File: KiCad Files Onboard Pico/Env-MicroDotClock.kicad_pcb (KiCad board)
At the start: 2 copper layers, 110 x 80 mm, 105 parts, among them IC1 IS31FL3730-QFLS2-TR, IC2 IS31FL3730-QFLS2-TR, IC3 IS31FL3730-QFLS2-TR, IC4 IS31FL3730-QFLS2-TR, J1 Conn_01x06_Pin, J3 Button, M1 Dip-14 Socket, M2 Dip-14 Socket, M3 Dip-14 Socket, M4 Dip-14 Socket, M5 Dip-14 Socket, M6 Dip-14 Socket, M7 Dip-14 Socket, M8 Dip-14 Socket, Q1 2SC1815, SW1 SW_Push, SW2 SW_Push, SW3 SW_Push, SW4 SW_Push, SW5 SW_Push, U1 Si7021-A20, U2 SOT-23-5 5.5V 3.3V 500mA, U3 DS3231M, U4 RP2040, Y1 3225_4P 12MHz

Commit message: sync push
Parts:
- moved R21 28.8 mm to (93.5, 47.0)
- moved R4 27.4 mm to (55.5, 69.5), turned to 180 degrees
- moved C30 27.0 mm to (89.9, 59.1)
- moved C31 27.0 mm to (89.9, 61.1)
- moved C26 27.0 mm to (87.0, 61.1)
- moved C27 27.0 mm to (87.0, 63.0)
- moved C28 27.0 mm to (87.0, 65.0)
- moved C29 27.0 mm to (87.0, 67.0)
- moved C24 27.0 mm to (84.1, 67.0)
- moved R3 26.9 mm to (55.5, 63.0)
- moved R18 17.8 mm to (121.0, 79.5), turned to 0 degrees
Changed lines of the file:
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@@
   (net 154 "unconnected-(U1-PAD-Pad7)")
   (footprint "Resistor_SMD:R_0805_2012Metric" (layer "F.Cu")
-    (at 82.27 60.85)
+    (at 55.5 63)
     (descr "Resistor SMD 0805 (2012 Metric), square (rectangular) end terminal, IPC_7351 nominal, (Body size source: IPC-SM-782 page 72, https://www.pcb-3d.com/wordpress/wp-content/uploads/ipc-sm-782a_amendment_1_and_2.pdf), generated with kicad-footprint-generator")
     (tags "resistor")
@@
   )
   (footprint "Capacitor_SMD:C_0402_1005Metric" (layer "F.Cu")
-    (at 61.525 56.125)
+    (at 87 65)
     (descr "Capacitor SMD 0402 (1005 Metric), square (rectangular) end terminal, IPC_7351 nominal, (Body size source: IPC-SM-782 page 76, https://www.pcb-3d.com/wordpress/wp-content/uploads/ipc-sm-782a_amendment_1_and_2.pdf), generated with kicad-footprint-generator")
     (tags "capacitor")
@@
   )
   (footprint "Resistor_SMD:R_0402_1005Metric" (layer "F.Cu")
-    (at 108.1 67.19 90)
+    (at 121 79.5)
     (descr "Resistor SMD 0402 (1005 Metric), square (rectangular) end terminal, IPC_7351 nominal, (Body size source: IPC-SM-782 page 72, https://www.pcb-3d.com/wordpress/wp-content/uploads/ipc-sm-782a_amendment_1_and_2.pdf), generated with kicad-footprint-generator")
     (tags "resistor")
@@
     (property "ki_keywords" "R res resistor")
     (attr smd)
-    (fp_text reference "R18" (at 0 -1.17 90) (layer "F.SilkS")
+    (fp_text reference "R18" (at 0 -1.17) (layer "F.SilkS")
         (effects (font (size 1 1) (thickness 0.15)))
     )
-    (fp_text value "1K 0402" (at 0 1.17 90) (layer "F.Fab")
+    (fp_text value "1K 0402" (at 0 1.17) (layer "F.Fab")
         (effects (font (size 1 1) (thickness 0.15)))
     )
-    (fp_text user "${REFERENCE}" (at 0 0 90) (layer "F.Fab")
+    (fp_text user "${REFERENCE}" (at 0 0) (layer "F.Fab")
         (effects (font (size 0.26 0.26) (thickness 0.04)))
     )
@@
     (fp_line (start 0.525 0.27) (end -0.525 0.27)
       (stroke (width 0.1) (type solid)) (layer "F.Fab"))
-    (pad "1" smd roundrect (at -0.51 0 90) (size 0.54 0.64) (layers "F.Cu" "F.Paste" "F.Mask") (roundrect_rratio 0.25)
+    (pad "1" smd roundrect (at -0.51 0) (size 0.54 0.64) (layers "F.Cu" "F.Paste" "F.Mask") (roundrect_rratio 0.25)
       (net 16 "/Onboard Pico/QSPI_SS") (pintype "passive"))
-    (pad "2" smd roundrect (at 0.51 0 90) (size 0.54 0.64) (layers "F.Cu" "F.Paste" "F.Mask") (roundrect_rratio 0.25)
+    (pad "2" smd roundrect (at 0.51 0) (size 0.54 0.64) (layers "F.Cu" "F.Paste" "F.Mask") (roundrect_rratio 0.25)
       (net 101 "/Onboard Pico/~{USB_BOOT}") (pintype "passive"))
     (model "${KICAD6_3DMODEL_DIR}/Resistor_SMD.3dshapes/R_0402_1005Metric.wrl"
@@
   )
   (footprint "Capacitor_SMD:C_0402_1005Metric" (layer "F.Cu")
-    (at 64.395 52.185)
+    (at 89.87 61.06)
     (descr "Capacitor SMD 0402 (1005 Metric), square (rectangular) end terminal, IPC_7351 nominal, (Body size source: IPC-SM-782 page 76, https://www.pcb-3d.com/wordpress/wp-content/uploads/ipc-sm-782a_amendment_1_and_2.pdf), generated with kicad-footprint-generator")
     (tags "capacitor")
@@
   )
   (footprint "Capacitor_SMD:C_0402_1005Metric" (layer "F.Cu")
-    (at 61.525 52.185)
+    (at 87 61.06)
     (descr "Capacitor SMD 0402 (1005 Metric), square (rectangular) end terminal, IPC_7351 nominal, (Body size source: IPC-SM-782 page 76, https://www.pcb-3d.com/wordpress/wp-content/uploads/ipc-sm-782a_amendment_1_and_2.pdf), generated with kicad-footprint-generator")
     (tags "capacitor")
@@
   )
   (footprint "Capacitor_SMD:C_0402_1005Metric" (layer "F.Cu")
-    (at 61.525 58.095)
+    (at 87 66.97)
     (descr "Capacitor SMD 0402 (1005 Metric), square (rectangular) end terminal, IPC_7351 nominal, (Body size source: IPC-SM-782 page 76, https://www.pcb-3d.com/wordpress/wp-content/uploads/ipc-sm-782a_amendment_1_and_2.pdf), generated with kicad-footprint-generator")
     (tags "capacitor")
@@
   )
   (footprint "Capacitor_SMD:C_0402_1005Metric" (layer "F.Cu")
-    (at 64.395 50.215)
+    (at 89.87 59.09)
     (descr "Capacitor SMD 0402 (1005 Metric), square (rectangular) end terminal, IPC_7351 nominal, (Body size source: IPC-SM-782 page 76, https://www.pcb-3d.com/wordpress/wp-content/uploads/ipc-sm-782a_amendment_1_and_2.pdf), generated with kicad-footprint-generator")
     (tags "capacitor")
@@
   )
   (footprint "Resistor_SMD:R_0402_1005Metric" (layer "F.Cu")
-    (at 114.07 67.19 90)
+    (at 93.5 47 90)
     (descr "Resistor SMD 0402 (1005 Metric), square (rectangular) end terminal, IPC_7351 nominal, (Body size source: IPC-SM-782 page 72, https://www.pcb-3d.com/wordpress/wp-content/uploads/ipc-sm-782a_amendment_1_and_2.pdf), generated with kicad-footprint-generator")
     (tags "resistor")
@@
   )
   (footprint "Resistor_SMD:R_0805_2012Metric" (layer "F.Cu")
-    (at 82.27 63.8)
+    (at 55.5 69.5 180)
     (descr "Resistor SMD 0805 (2012 Metric), square (rectangular) end terminal, IPC_7351 nominal, (Body size source: IPC-SM-782 page 72, https://www.pcb-3d.com/wordpress/wp-content/uploads/ipc-sm-782a_amendment_1_and_2.pdf), generated with kicad-footprint-generator")
     (tags "resistor")
@@
     (fp_line (start 1 0.625) (end -1 0.625)
       (stroke (width 0.1) (type solid)) (layer "F.Fab"))
-    (pad "1" smd roundrect (at -0.9125 0) (size 1.025 1.4) (layers "F.Cu" "F.Paste" "F.Mask") (roundrect_rratio 0.243902)
+    (pad "1" smd roundrect (at -0.9125 0 180) (size 1.025 1.4) (layers "F.Cu" "F.Paste" "F.Mask") (roundrect_rratio 0.243902)
       (net 109 "Buzzer GPIO") (pintype "passive"))
-    (pad "2" smd roundrect (at 0.9125 0) (size 1.025 1.4) (layers "F.Cu" "F.Paste" "F.Mask") (roundrect_rratio 0.243902)
+    (pad "2" smd roundrect (at 0.9125 0 180) (size 1.025 1.4) (layers "F.Cu" "F.Paste" "F.Mask") (roundrect_rratio 0.243902)
       (net 108 "Net-(Q1-B)") (pintype "passive"))
     (model "${KICAD6_3DMODEL_DIR}/Resistor_SMD.3dshapes/R_0805_2012Metric.wrl"
@@
   )
   (footprint "Capacitor_SMD:C_0402_1005Metric" (layer "F.Cu")
-    (at 61.525 54.155)
+    (at 87 63.03)
     (descr "Capacitor SMD 0402 (1005 Metric), square (rectangular) end terminal, IPC_7351 nominal, (Body size source: IPC-SM-782 page 76, https://www.pcb-3d.com/wordpress/wp-content/uploads/ipc-sm-782a_amendment_1_and_2.pdf), generated with kicad-footprint-generator")
     (tags "capacitor")
@@
   )
   (footprint "Capacitor_SMD:C_0402_1005Metric" (layer "F.Cu")
-    (at 58.655 58.095)
+    (at 84.13 66.97)
     (descr "Capacitor SMD 0402 (1005 Metric), square (rectangular) end terminal, IPC_7351 nominal, (Body size source: IPC-SM-782 page 76, https://www.pcb-3d.com/wordpress/wp-content/uploads/ipc-sm-782a_amendment_1_and_2.pdf), generated with kicad-footprint-generator")
     (tags "capacitor")

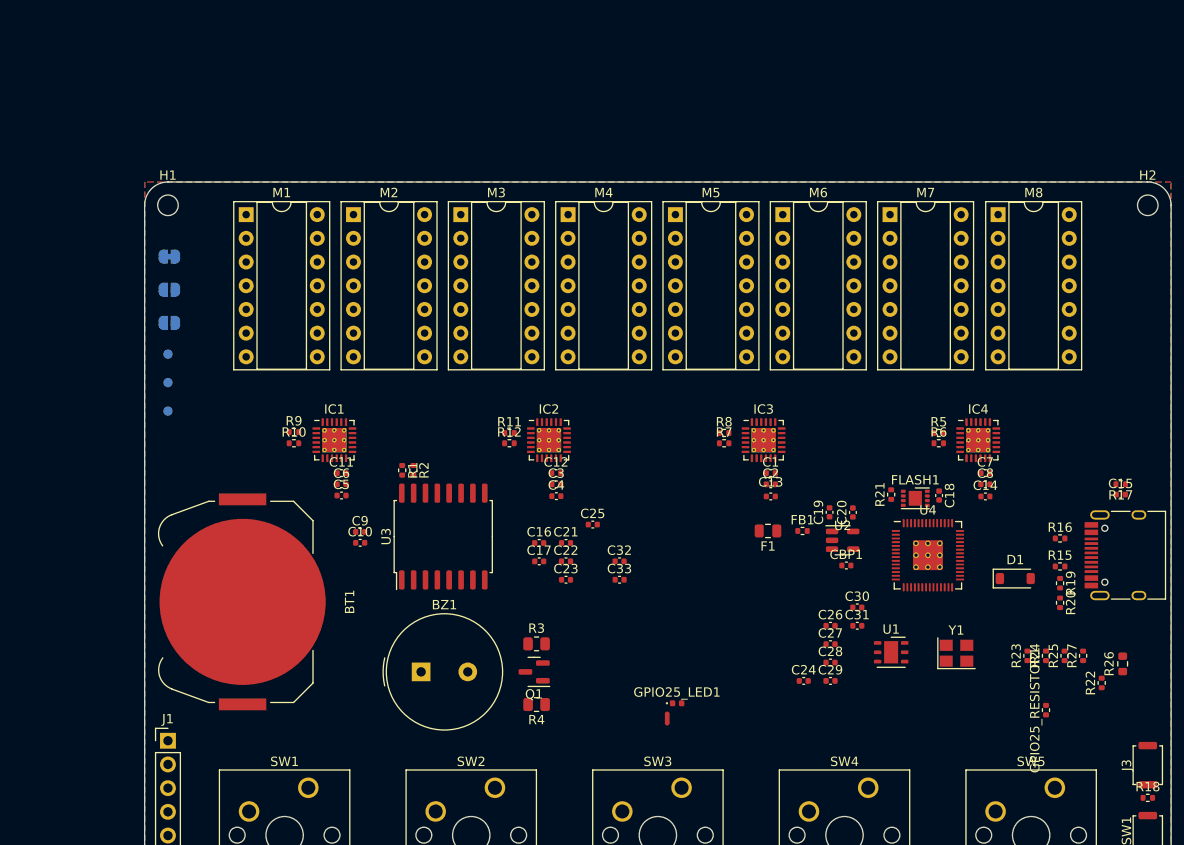
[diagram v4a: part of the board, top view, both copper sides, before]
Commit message: Finished V1 Placement of onboard pico
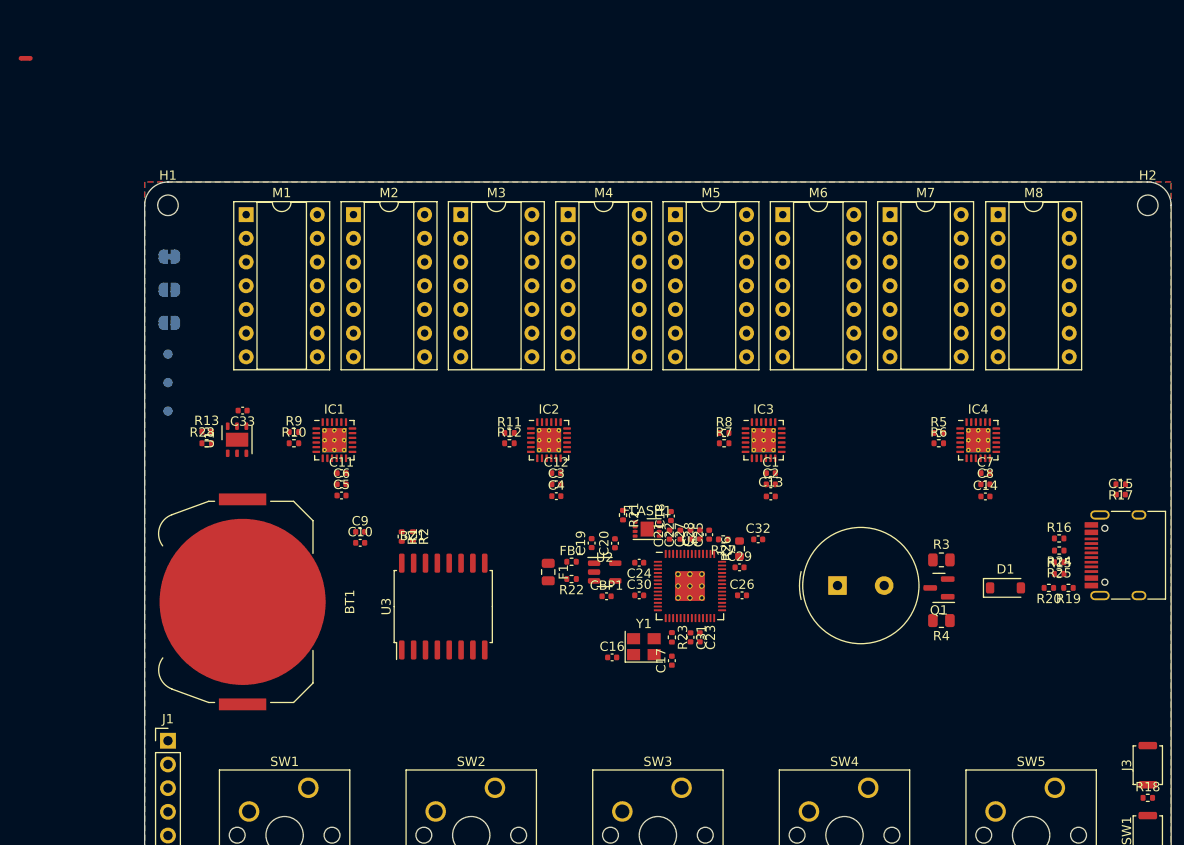
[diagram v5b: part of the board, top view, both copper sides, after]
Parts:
- removed GPIO25_LED1: LED_0402, LED_SMD:LED_0402_1005Metric
- removed GPIO25_RESISTOR1: 470 0402, Resistor_SMD:R_0402_1005Metric
- added R13: 0402 10K, Resistor_SMD:R_0402_1005Metric, F.Cu at (20.1, 40.2)
- added R28: 0402 10K, Resistor_SMD:R_0402_1005Metric, F.Cu at (20.1, 41.5)
- C33: value 10uf 0402 -> 0402 0.1uF
- moved NT1 98.7 mm to (0.75, 0.25), turned to 0 degrees
- moved U1 73.7 mm to (23.4, 41.1), turned to 90 degrees
- moved R22 57.9 mm to (59.2, 56.0), turned to 180 degrees
- moved BZ1 45.6 mm to (87.8, 56.8)
- moved R3 44.3 mm to (98.9, 54.0)
- moved R4 44.3 mm to (98.9, 60.5)
- moved Q1 44.3 mm to (98.6, 57.0)
- moved C33 44.3 mm to (24.0, 38.0), turned to 180 degrees
- moved R26 42.9 mm to (77.2, 52.8)
- moved R27 40.5 mm to (75.5, 51.8), turned to 180 degrees
- moved R23 38.2 mm to (70.0, 62.3), turned to -90 degrees
- moved Y1 33.5 mm to (67.0, 63.3)
- moved FLASH1 28.9 mm to (67.3, 50.7)
- moved C18 28.8 mm to (69.9, 49.3), turned to 90 degrees
- moved R21 28.8 mm to (64.8, 49.2), turned to -90 degrees
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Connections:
- BT1 pad 2: GND -> DEBUG-GND
- C1 pad 2: GND -> DEBUG-GND
- C10 pad 2: GND -> DEBUG-GND
- C11 pad 2: GND -> DEBUG-GND
- C12 pad 2: GND -> DEBUG-GND
- C13 pad 2: GND -> DEBUG-GND
- C14 pad 2: GND -> DEBUG-GND
- C15 pad 1: GND -> DEBUG-GND
- C16 pad 1: GND -> DEBUG-GND
- C17 pad 1: GND -> DEBUG-GND
- C18 pad 2: GND -> DEBUG-GND
- C19 pad 2: GND -> DEBUG-GND
- C2 pad 2: GND -> DEBUG-GND
- C20 pad 2: GND -> DEBUG-GND
- C21 pad 2: GND -> DEBUG-GND
- C22 pad 2: GND -> DEBUG-GND
- C23 pad 2: GND -> DEBUG-GND
- C24 pad 2: GND -> DEBUG-GND
- C25 pad 2: GND -> DEBUG-GND
- C26 pad 2: GND -> DEBUG-GND
- C27 pad 2: GND -> DEBUG-GND
- C28 pad 2: GND -> DEBUG-GND
- C29 pad 2: GND -> DEBUG-GND
- C3 pad 2: GND -> DEBUG-GND
- C30 pad 2: GND -> DEBUG-GND
- C31 pad 2: GND -> DEBUG-GND
- C32 pad 2: GND -> DEBUG-GND
- C33 pad 1: +3V3 -> DEBUG-GND
- C33 pad 2: GND -> +3V3
- C4 pad 2: GND -> DEBUG-GND
- C5 pad 2: GND -> DEBUG-GND
- C6 pad 2: GND -> DEBUG-GND
- C7 pad 2: GND -> DEBUG-GND
- C8 pad 2: GND -> DEBUG-GND
- C9 pad 2: GND -> DEBUG-GND
- CBP1 pad 2: GND -> DEBUG-GND
- FLASH1 pad 4: GND -> DEBUG-GND
- FLASH1 pad 9: GND -> DEBUG-GND
- IC1 pad 1: GPIO0 -> GPIO16
- IC1 pad 2: GPIO1 -> GPIO17
- IC1 pad 20: GND -> DEBUG-GND
- IC1 pad 25: GND -> DEBUG-GND
- IC2 pad 20: GND -> DEBUG-GND
- IC2 pad 25: GND -> DEBUG-GND
- IC2 pad 6: GND -> DEBUG-GND
- IC3 pad 20: GND -> DEBUG-GND
- IC3 pad 25: GND -> DEBUG-GND
- IC4 pad 20: GND -> DEBUG-GND
- IC4 pad 25: GND -> DEBUG-GND
- J1 pad 1: RX -> GPIO1
- J1 pad 2: GND -> DEBUG-GND
- J1 pad 3: TX -> GPIO0
- J3 pad 2: GND -> DEBUG-GND
- NT1 pad 1: GND -> DEBUG-GND
- Q1 pad 2: GND -> DEBUG-GND
- R10 pad 2: GPIO1 -> GPIO17
- R15 pad 1: GND -> DEBUG-GND
- R16 pad 1: GND -> DEBUG-GND
- R17 pad 2: GND -> DEBUG-GND
- R20 pad 2: GND -> DEBUG-GND
- R9 pad 2: GPIO0 -> GPIO16
- RSW1 pad 1: GND -> DEBUG-GND
- SW1 pad 2: GND -> DEBUG-GND
- SW2 pad 2: GND -> DEBUG-GND
- SW3 pad 2: GND -> DEBUG-GND
- SW4 pad 2: GND -> DEBUG-GND
- SW5 pad 2: GND -> DEBUG-GND
- U1 pad 2: GND -> DEBUG-GND
- U2 pad 2: GND -> DEBUG-GND
- U3 pad 10: GND -> DEBUG-GND
- U3 pad 11: GND -> DEBUG-GND
- U3 pad 12: GND -> DEBUG-GND
- U3 pad 13: GND -> DEBUG-GND
- U3 pad 5: GND -> DEBUG-GND
- U3 pad 6: GND -> DEBUG-GND
- U3 pad 7: GND -> DEBUG-GND
- U3 pad 8: GND -> DEBUG-GND
- U3 pad 9: GND -> DEBUG-GND
- U4 pad 19: GND -> DEBUG-GND
- U4 pad 24: /Onboard Pico/SWCLK -> SWCLK
- U4 pad 25: /Onboard Pico/SWD -> SWDIO
- U4 pad 57: GND -> DEBUG-GND
- USB1 pad 1: GND -> DEBUG-GND
- USB1 pad 12: GND -> DEBUG-GND
- Y1 pad 2: GND -> DEBUG-GND
- Y1 pad 4: GND -> DEBUG-GND
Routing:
- added copper zone on B.Cu, net DEBUG-GND
- added copper zone on F.Cu, net DEBUG-GND
- removed copper zone on B.Cu, net GND
- removed copper zone on F.Cu, net GND

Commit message: Finished V2 placement and base wireing of RP2040
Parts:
- removed C32: 2.2uF 0402, Capacitor_SMD:C_0402_1005Metric
- removed R26: 200 0603, Resistor_SMD:R_0603_1608Metric
- removed R27: 1 0402, Resistor_SMD:R_0402_1005Metric
- moved R18 51.9 mm to (77.0, 52.0)
- moved R24 41.0 mm to (71.1, 60.2)
- moved R25 41.0 mm to (71.1, 61.2)
- moved FB1 23.9 mm to (79.9, 66.2), turned to 90 degrees
- moved F1 23.6 mm to (76.5, 68.3), turned to 180 degrees
- moved C19 21.8 mm to (79.9, 63.8)
- moved R22 21.4 mm to (80.0, 61.3), turned to -90 degrees
- moved C20 18.9 mm to (76.5, 66.2), turned to 0 degrees
- moved C28 16.8 mm to (58.1, 59.2), turned to 180 degrees
- moved C27 16.6 mm to (63.6, 65.7), turned to -90 degrees
- moved U2 15.9 mm to (76.5, 63.2), turned to 180 degrees
- moved C17 15.6 mm to (56.1, 57.6), turned to 0 degrees
- moved C23 15.0 mm to (58.1, 60.2), turned to 180 degrees
- moved C16 14.9 mm to (56.1, 51.6), turned to 180 degrees
- moved C29 14.4 mm to (63.1, 52.2), turned to 90 degrees
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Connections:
- U4 pad 43: Net-(U4-ADC_AVDD) -> +3V3
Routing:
- net +3V3: track 0.00 -> 101.5 mm, vias 0 -> 4
- net Net-(BT1-+): track 0.00 -> 35.9 mm
- net Net-(USB1-SHIELD): track 0.00 -> 20.9 mm
- net VCC: track 0.00 -> 17.0 mm
- net +1V1: track 0.00 -> 12.8 mm, vias 0 -> 2
- net VSYS: track 0.00 -> 12.6 mm
- net XIN: track 0.00 -> 10.9 mm
- net /Onboard Pico/QSPI_SS: track 0.00 -> 10.6 mm
- net /Onboard Pico/QSPI_SD1: track 0.00 -> 9.97 mm
- net /Onboard Pico/QSPI_SD2: track 0.00 -> 9.39 mm
- net /Onboard Pico/QSPI_SD3: track 0.00 -> 7.84 mm
- net GPIO8: track 0.00 -> 7.31 mm
- net /Onboard Pico/QSPI_SCLK: track 0.00 -> 7.18 mm
- net /Onboard Pico/QSPI_SD0: track 0.00 -> 6.39 mm
- net GPIO13: track 0.00 -> 4.39 mm
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- added copper zone on F.Cu, net +1V1
- added copper zone on B.Cu, net +3V3
- added copper zone on F.Cu, net +3V3
- added copper zone on F.Cu, net /Onboard Pico/QSPI_SS
- added copper zone on F.Cu, net Net-(C17-Pad2)

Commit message: fulkly wired v2
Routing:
- net /Onboard Pico/~{USB_BOOT}: track 0.00 -> 187.2 mm, vias 0 -> 4
- net +3V3: track 101.5 -> 235.2 mm, vias 4 -> 17
- net USB_D+: track 0.00 -> 131.8 mm, vias 0 -> 4
- net USB_D-: track 0.00 -> 131.0 mm, vias 0 -> 3
- net VBUS: track 0.00 -> 126.3 mm, vias 0 -> 1
- net VCC: track 17.0 -> 130.1 mm, vias 0 -> 1
- net GPIO6: track 2.37 -> 102.3 mm, vias 0 -> 1
- net GPIO3: track 1.98 -> 89.2 mm, vias 0 -> 3
- net GPIO2: track 2.19 -> 83.3 mm, vias 0 -> 2
- net IC1R3: track 0.00 -> 75.8 mm, vias 0 -> 2
- net GPIO0: track 0.00 -> 71.5 mm, vias 0 -> 2
- net /Onboard Pico/RUN: track 0.00 -> 71.1 mm
- net IC4R4: track 0.00 -> 65.3 mm, vias 0 -> 1
- net SWCLK: track 0.00 -> 61.8 mm, vias 0 -> 2
- net IC2R3: track 0.00 -> 60.1 mm, vias 0 -> 2
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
